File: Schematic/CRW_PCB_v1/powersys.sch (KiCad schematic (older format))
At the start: 30 parts

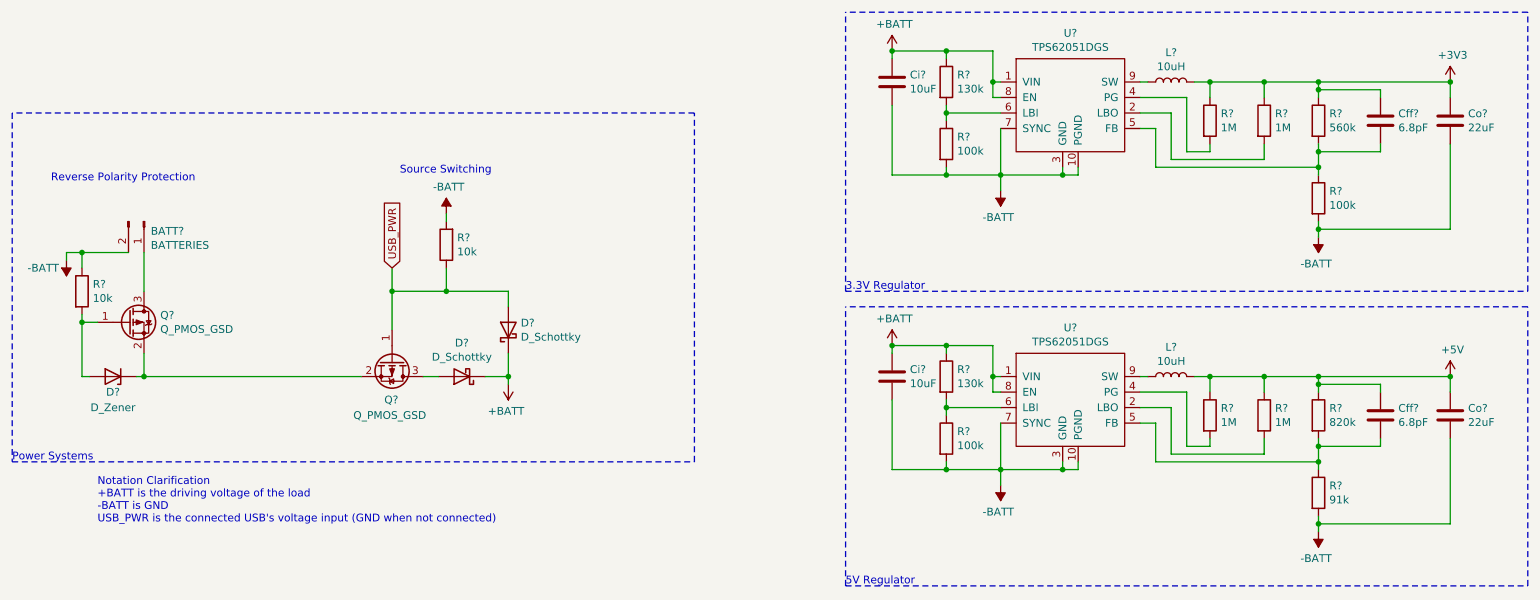
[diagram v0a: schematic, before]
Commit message: Added Hotwire Connection
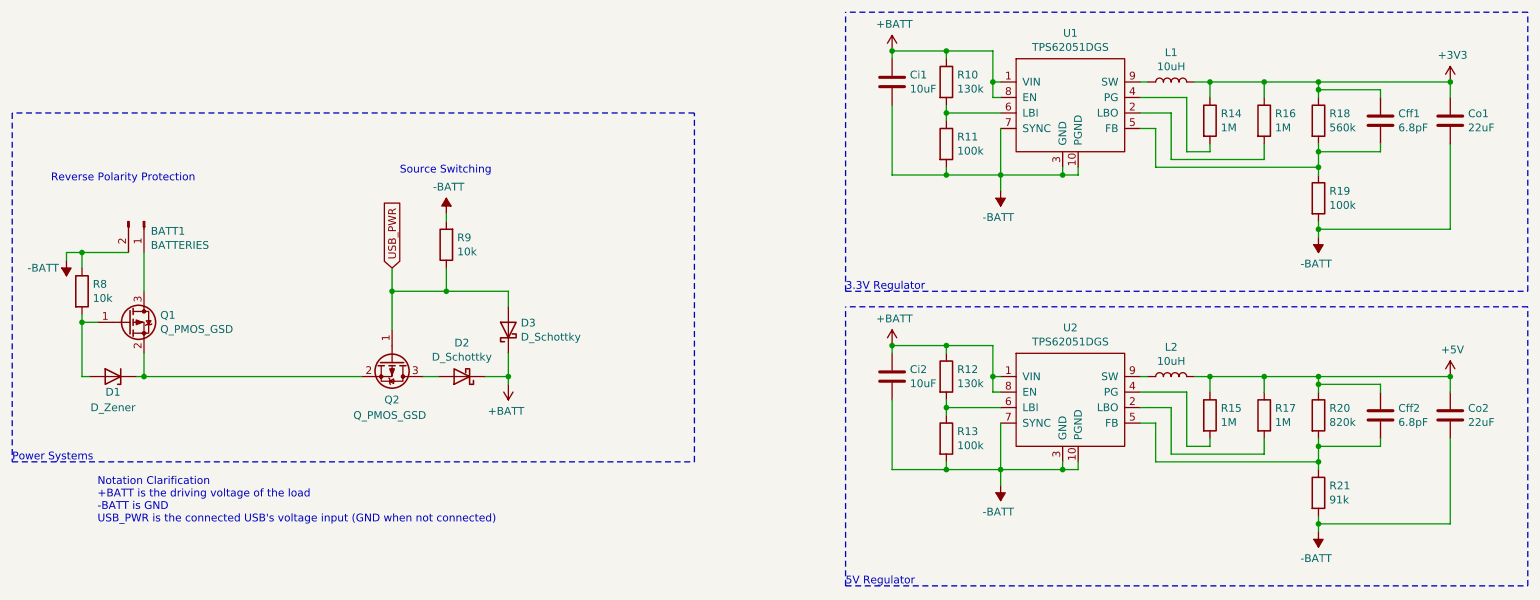
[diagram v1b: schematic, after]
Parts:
- gave numbers to parts that had none: 30
